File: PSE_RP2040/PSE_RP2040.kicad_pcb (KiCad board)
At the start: 2 copper layers, 100 x 60 mm, 127 parts, among them IC1 LAN8742A-CZ, IC2 SAM-M8Q-0, J1 USB_B, J2 USB_B_Mini, J3 8P8C_LED, J4 Conn_01x03, J5 Screw_Terminal_01x02, J6 Conn_01x04_Female, Q2 IRLML6402, SW1 SW_Push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

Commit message: pcb parz. Aggiornato
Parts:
- moved TP5 29.2 mm to (138.0, 148.8)
- moved TP6 24.6 mm to (134.4, 148.2)
- moved C28 11.6 mm to (138.1, 154.2), turned to 90 degrees
- moved R30 9.12 mm to (141.4, 156.6)
- moved D2 4.16 mm to (132.6, 155.8), turned to 180 degrees
- moved R33 4.13 mm to (138.1, 151.1), turned to 90 degrees
- moved R38 3.78 mm to (139.7, 154.3), turned to -90 degrees
- moved D3 3.68 mm to (132.6, 151.5), turned to 180 degrees
- moved R31 3.12 mm to (146.5, 147.6)
- moved R29 3.01 mm to (146.5, 146.0)
- moved R32 2.20 mm to (139.7, 151.1), turned to -90 degrees
- moved U7 0.29 mm to (145.8, 152.5)
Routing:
- net poe+: track 0.00 -> 26.0 mm
- net poe-: track 0.00 -> 21.3 mm
- net RJ45_RXC: track 0.00 -> 16.9 mm
- net RJ45_TXC: track 0.00 -> 12.9 mm
- net Net-(R30-Pad1): track 0.00 -> 9.28 mm, vias 0 -> 2
- net Net-(D2-Pad4): track 27.7 -> 34.5 mm, vias 0 -> 2
- net Net-(R32-Pad1): track 0.00 -> 3.64 mm
- net Net-(R29-Pad2): track 0.00 -> 1.60 mm
- net Net-(R32-Pad2): track 0.00 -> 1.60 mm
- net Net-(D2-Pad3): track 30.0 -> 29.7 mm, vias 0 -> 1
- net TX_P: track 13.3 -> 13.4 mm, vias 1 -> 0
- net TX_N: vias 1 -> 0

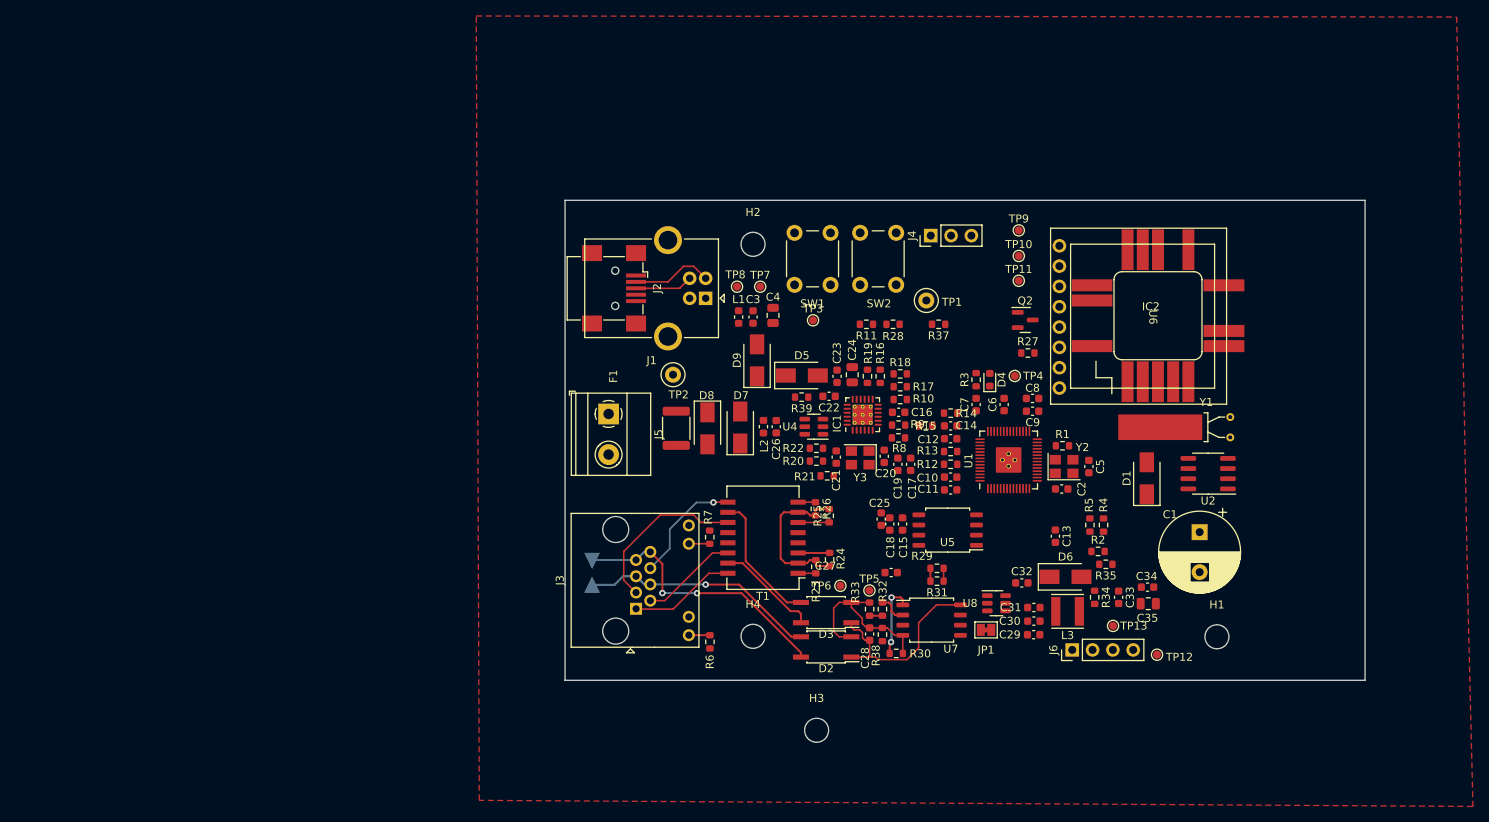
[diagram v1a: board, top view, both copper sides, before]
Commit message: PCB
Sbroglio parte alimentazione
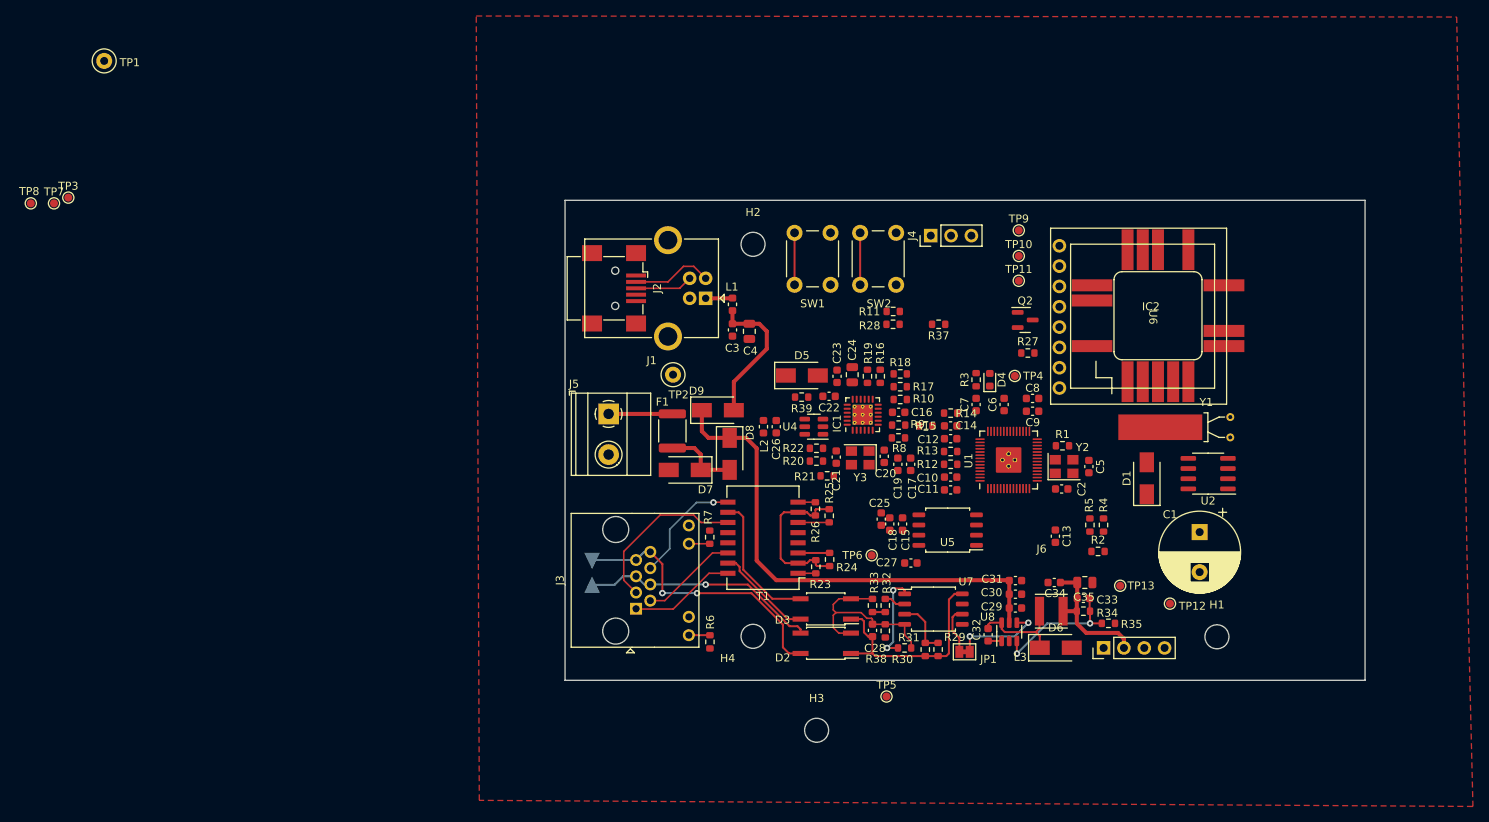
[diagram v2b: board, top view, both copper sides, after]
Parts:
- moved TP1 107.0 mm to (42.4, 82.6)
- moved TP3 94.3 mm to (37.9, 99.7)
- moved TP7 88.9 mm to (36.1, 100.4)
- moved TP8 88.9 mm to (33.2, 100.4)
- moved TP5 13.4 mm to (140.2, 162.0)
- moved C34 11.7 mm to (161.2, 147.8), turned to 180 degrees
- moved R29 10.1 mm to (146.6, 156.1), turned to 90 degrees
- moved D6 8.95 mm to (161.3, 155.9)
- moved D7 8.74 mm to (115.0, 133.7), turned to 180 degrees
- moved R31 8.67 mm to (145.0, 156.2), turned to 90 degrees
- moved C35 8.36 mm to (165.0, 147.8)
- moved D9 7.93 mm to (119.1, 126.2), turned to 0 degrees
- moved C32 7.73 mm to (152.9, 154.3), turned to 90 degrees
- moved R35 7.39 mm to (167.9, 152.9), turned to 0 degrees
- moved TP12 6.58 mm to (175.6, 150.4)
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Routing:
- net Net-(C29-Pad1): track 0.00 -> 62.3 mm
- net +5V: track 0.00 -> 18.4 mm
- net Net-(C33-Pad2): track 0.00 -> 16.9 mm, vias 0 -> 2
- net +3V3: track 0.00 -> 16.8 mm
- net Net-(C32-Pad2): track 0.00 -> 12.5 mm
- net Net-(JP1-Pad2): track 0.00 -> 11.4 mm, vias 0 -> 2
- net Net-(D7-Pad1): track 0.00 -> 9.46 mm
- net Net-(F1-Pad1): track 0.00 -> 7.97 mm
- net Net-(R11-Pad2): track 0.00 -> 6.50 mm
- net /MCU_nRST: track 0.00 -> 6.50 mm
- net Net-(JP1-Pad1): track 0.00 -> 6.07 mm
- net Net-(R29-Pad2): track 1.60 -> 7.21 mm
- net /VUSB: track 0.00 -> 3.37 mm
- net poe-: track 21.3 -> 24.1 mm
- net Net-(C32-Pad1): track 0.00 -> 1.69 mm
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
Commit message: PCB
Aggiunto strato rame bottom, tolto mounting hole 4 dallo schematico, aggiunti fiducial (solo sul PCB), riduzione margine scheda, sbroglio.
(larghezza max piste in uscita dal micro 7 mils)
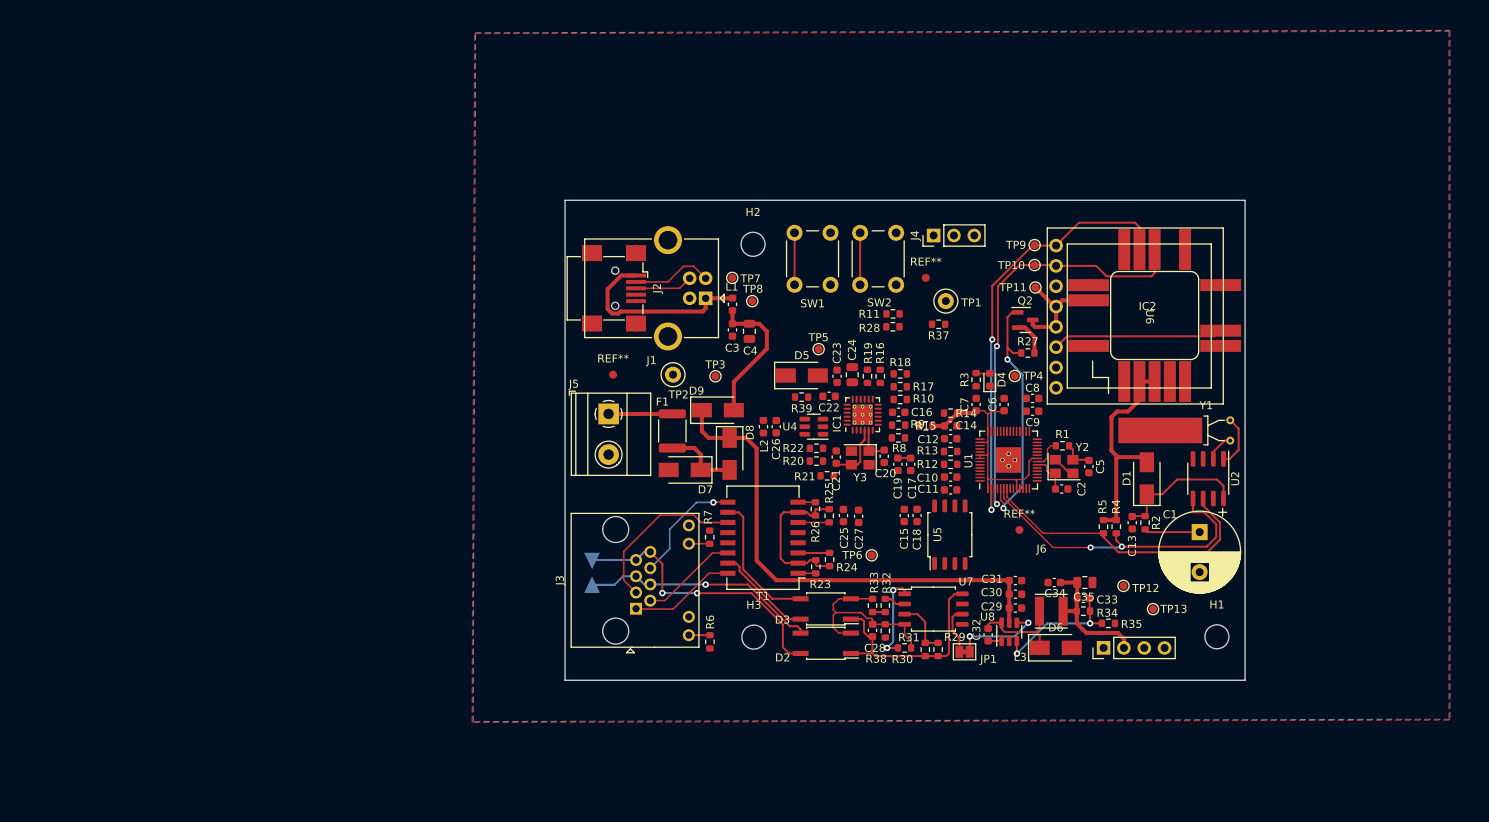
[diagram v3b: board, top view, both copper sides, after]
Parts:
- removed H4: MountingHole, MountingHole:MountingHole_3mm
- added REF**: Fiducial_1mm_Mask2mm, Fiducial:Fiducial_1mm_Mask2mm, F.Cu at (106.0, 121.8)
- added REF**: Fiducial_1mm_Mask2mm, Fiducial:Fiducial_1mm_Mask2mm, F.Cu at (145.1, 109.7)
- added REF**: Fiducial_1mm_Mask2mm, Fiducial:Fiducial_1mm_Mask2mm, F.Cu at (156.8, 141.2)
- moved TP1 109.4 mm to (147.6, 112.6)
- moved TP8 91.0 mm to (123.4, 112.6)
- moved TP7 85.3 mm to (120.9, 109.7)
- moved TP3 83.9 mm to (118.8, 122.0)
- moved TP5 44.2 mm to (131.7, 118.6)
- moved H3 14.0 mm to (123.6, 154.6)
- moved C13 9.76 mm to (170.9, 140.3)
- moved C27 8.76 mm to (136.7, 139.5), turned to -90 degrees
- moved R2 6.89 mm to (172.5, 140.3), turned to 90 degrees
- moved TP12 6.22 mm to (169.8, 148.2)
- moved TP13 5.04 mm to (173.5, 151.1)
- moved C25 4.74 mm to (134.8, 139.4)
- moved C18 3.57 mm to (144.0, 139.4), turned to -90 degrees
- moved TP9 2.71 mm to (158.7, 105.6)
- moved TP10 2.29 mm to (158.7, 108.1)
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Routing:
- net +3V3: track 16.8 -> 80.1 mm
- net /UART_TX-GPS_RX: track 0.00 -> 55.6 mm, vias 0 -> 2
- net /UART_RX-GPS_TX: track 0.00 -> 53.9 mm, vias 0 -> 2
- net /GPIO2_I2C_SDA: track 0.00 -> 39.5 mm, vias 0 -> 2
- net /GPIO3_I2C_SCL: track 0.00 -> 37.5 mm
- net /GPS_EN: track 0.00 -> 31.8 mm, vias 0 -> 2
- net /PPS: track 0.00 -> 21.4 mm
- net /VUSB: track 3.37 -> 24.1 mm
- net Net-(C13-Pad1): track 0.00 -> 16.7 mm
- net /VCC_GPS: track 0.00 -> 14.1 mm
- net Net-(C21-Pad1): track 0.00 -> 7.41 mm
- net Net-(C1-Pad1): track 0.00 -> 6.97 mm
- net Net-(U2-Pad1): track 0.00 -> 6.50 mm
- net Net-(C2-Pad1): track 0.00 -> 4.99 mm
- net Net-(C20-Pad1): track 0.00 -> 4.58 mm
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- added copper zone on B.Cu, net GND
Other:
- board size 100 x 60 mm -> 85 x 60 mm

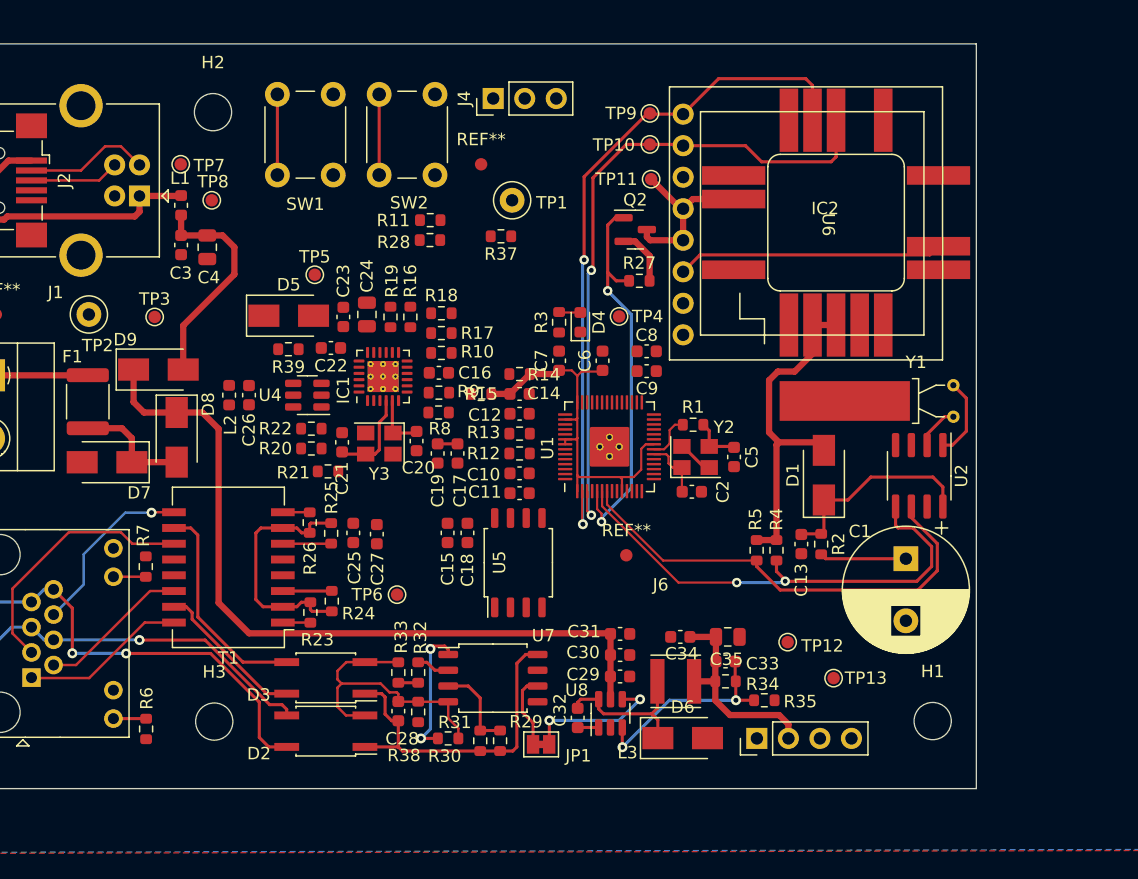
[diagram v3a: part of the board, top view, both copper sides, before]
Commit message: modifiche schematico e pcb
Invertito tx e rx  tra trasformatore e modulo lan per sbroglio più comodo.
Fatto posto per allontanare gps dal bordo e collegate varie cose
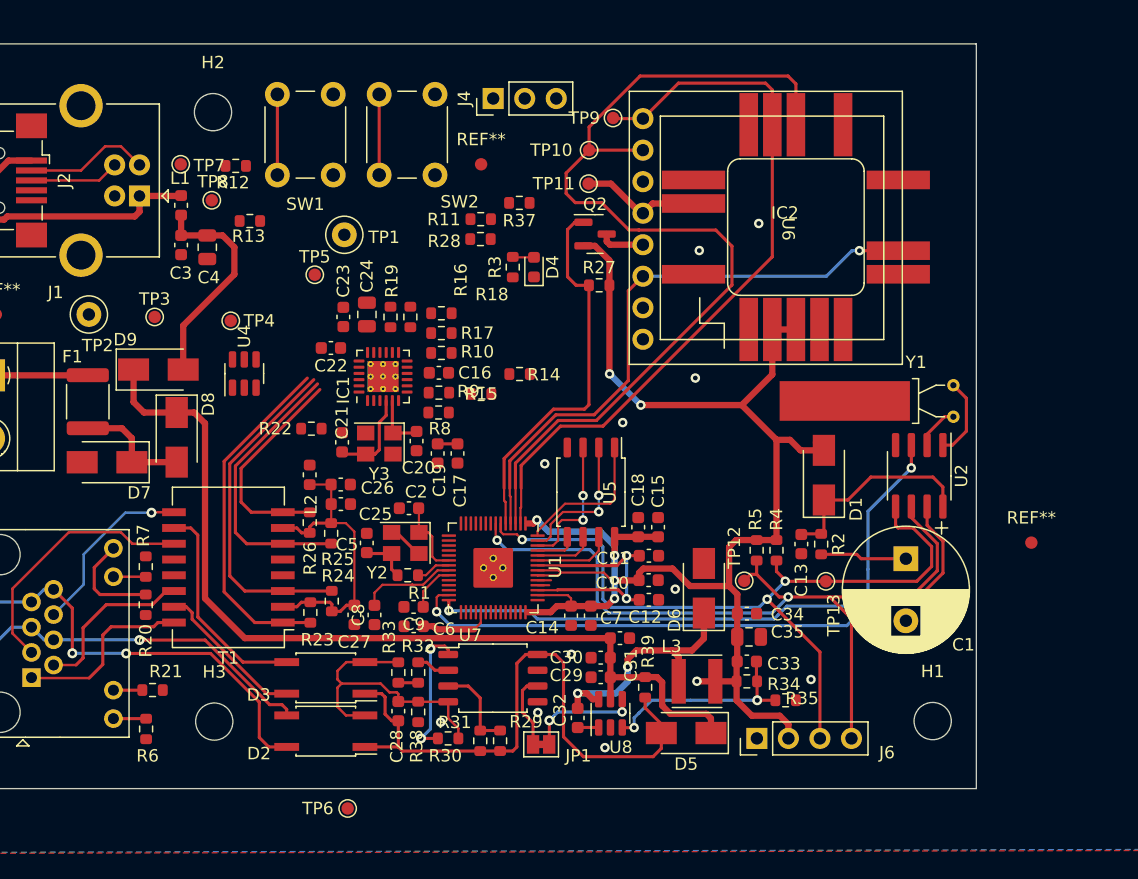
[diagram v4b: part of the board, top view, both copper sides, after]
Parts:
- moved D5 46.4 mm to (161.6, 155.5), turned to 180 degrees
- moved R39 39.6 mm to (158.3, 151.8), turned to 90 degrees
- moved REF** 32.6 mm to (189.4, 140.2)
- moved R12 32.6 mm to (125.3, 109.8)
- moved TP4 31.3 mm to (124.9, 122.3)
- moved C8 30.5 mm to (136.5, 146.0), turned to -90 degrees
- moved C5 30.4 mm to (135.9, 140.2), turned to 90 degrees
- moved R13 27.7 mm to (126.5, 114.3), turned to 180 degrees
- moved C9 26.7 mm to (139.7, 145.4)
- moved C6 26.3 mm to (139.7, 146.9), turned to 180 degrees
- moved R1 26.0 mm to (139.2, 142.8), turned to 180 degrees
- moved Y2 24.4 mm to (139.0, 140.2), turned to 180 degrees
- moved C2 22.8 mm to (139.3, 137.4), turned to 180 degrees
- moved R21 22.6 mm to (118.6, 152.1), turned to 0 degrees
- moved C7 20.7 mm to (153.9, 146.1), turned to -90 degrees
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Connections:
- R23 pad 1: Net-(IC1-Pad23) -> Net-(IC1-Pad21)
- R24 pad 1: Net-(IC1-Pad22) -> Net-(IC1-Pad20)
- R25 pad 1: Net-(IC1-Pad21) -> Net-(IC1-Pad23)
- R26 pad 1: Net-(IC1-Pad20) -> Net-(IC1-Pad22)
- T1 pad 1: Net-(IC1-Pad23) -> Net-(IC1-Pad21)
- T1 pad 3: Net-(IC1-Pad22) -> Net-(IC1-Pad20)
- T1 pad 6: Net-(IC1-Pad21) -> Net-(IC1-Pad23)
- T1 pad 8: Net-(IC1-Pad20) -> Net-(IC1-Pad22)
- U4 pad 1: Net-(IC1-Pad23) -> Net-(IC1-Pad21)
- U4 pad 3: Net-(IC1-Pad21) -> Net-(IC1-Pad23)
- U4 pad 4: Net-(IC1-Pad20) -> Net-(IC1-Pad22)
- U4 pad 6: Net-(IC1-Pad22) -> Net-(IC1-Pad20)
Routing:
- net +3V3: track 80.1 -> 136.4 mm, vias 0 -> 7
- net /RTC_nINT: track 0.00 -> 52.4 mm, vias 0 -> 2
- net /RTC_CLKOUT: track 0.00 -> 48.3 mm, vias 0 -> 2
- net /GPIO3_I2C_SCL: track 37.5 -> 66.7 mm, vias 0 -> 2
- net /PPS: track 21.4 -> 47.6 mm, vias 0 -> 1
- net Net-(IC1-Pad20): track 2.17 -> 27.4 mm
- net /UART_RX-GPS_TX: track 53.9 -> 78.9 mm, vias 2 -> 0
- net +1V1: track 0.00 -> 24.4 mm, vias 0 -> 2
- net /GPIO2_I2C_SDA: track 39.5 -> 63.6 mm, vias 2 -> 3
- net Net-(IC1-Pad21): track 3.90 -> 28.0 mm
- net poe+: track 27.7 -> 49.5 mm
- net Net-(IC1-Pad23): track 2.22 -> 22.8 mm
- net Net-(IC1-Pad22): track 3.95 -> 17.6 mm
- net /QSPI_SS: track 0.00 -> 11.8 mm
- net /QSPI_SD1: track 0.00 -> 11.7 mm, vias 0 -> 2
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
